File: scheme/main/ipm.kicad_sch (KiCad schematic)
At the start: 1 part

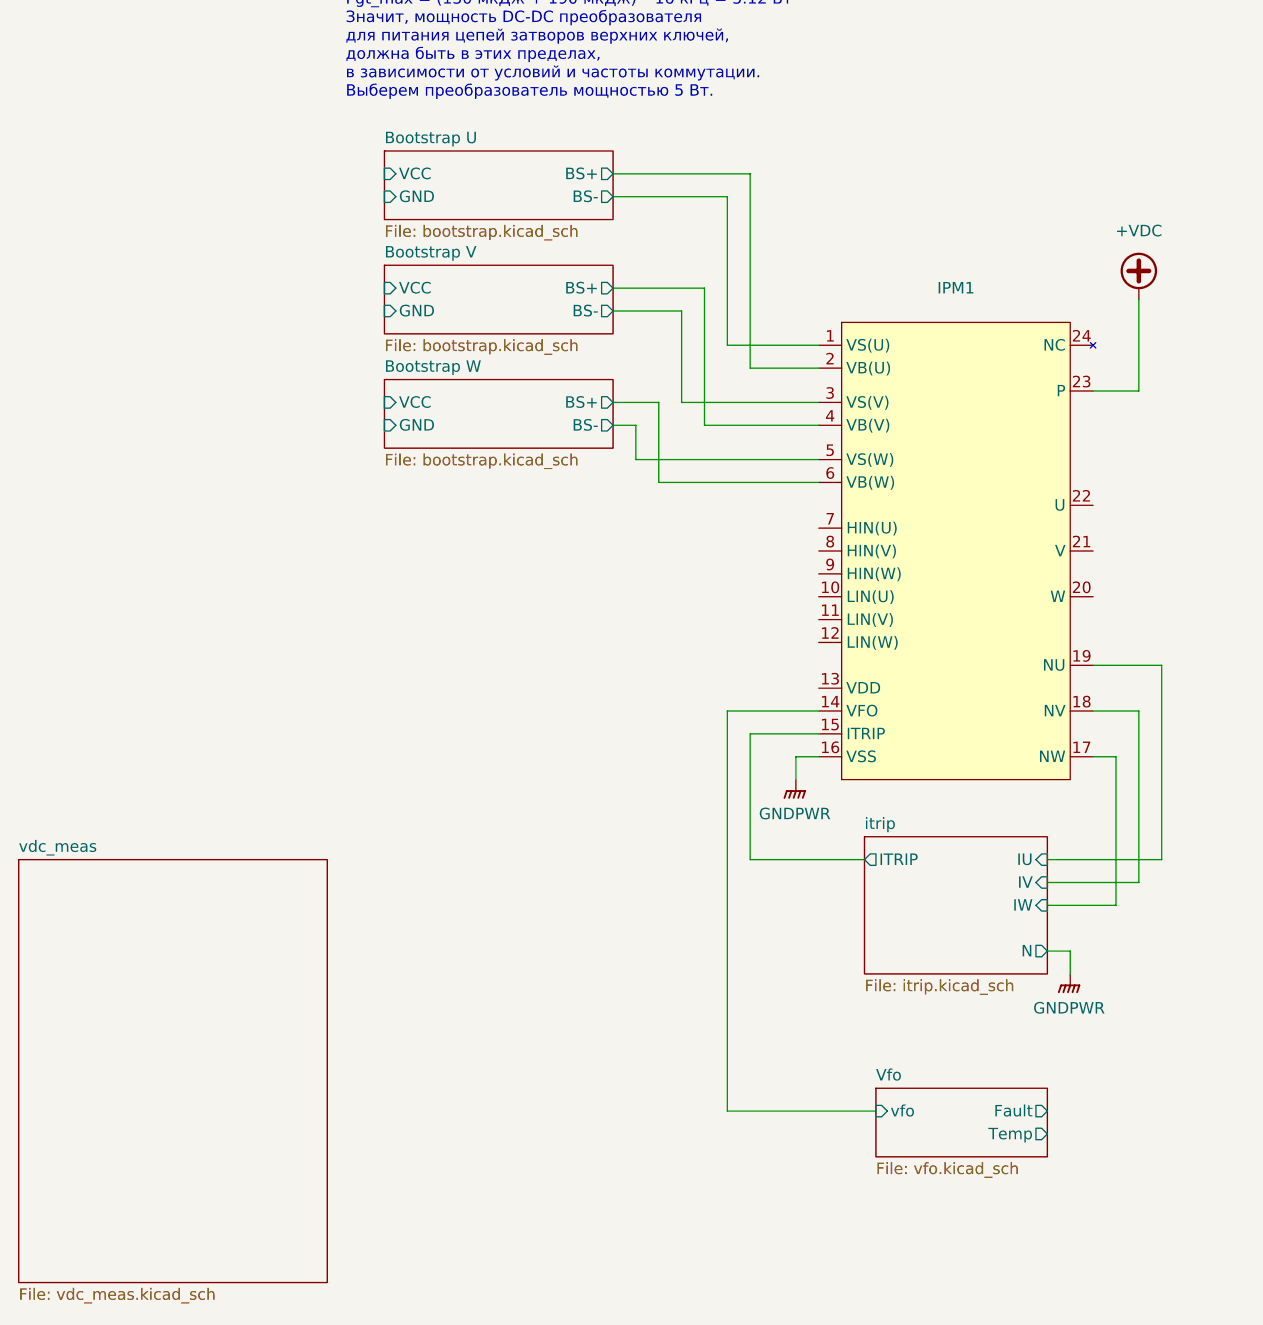
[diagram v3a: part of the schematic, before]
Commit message: bootstrap dc-dc add capacitors & more
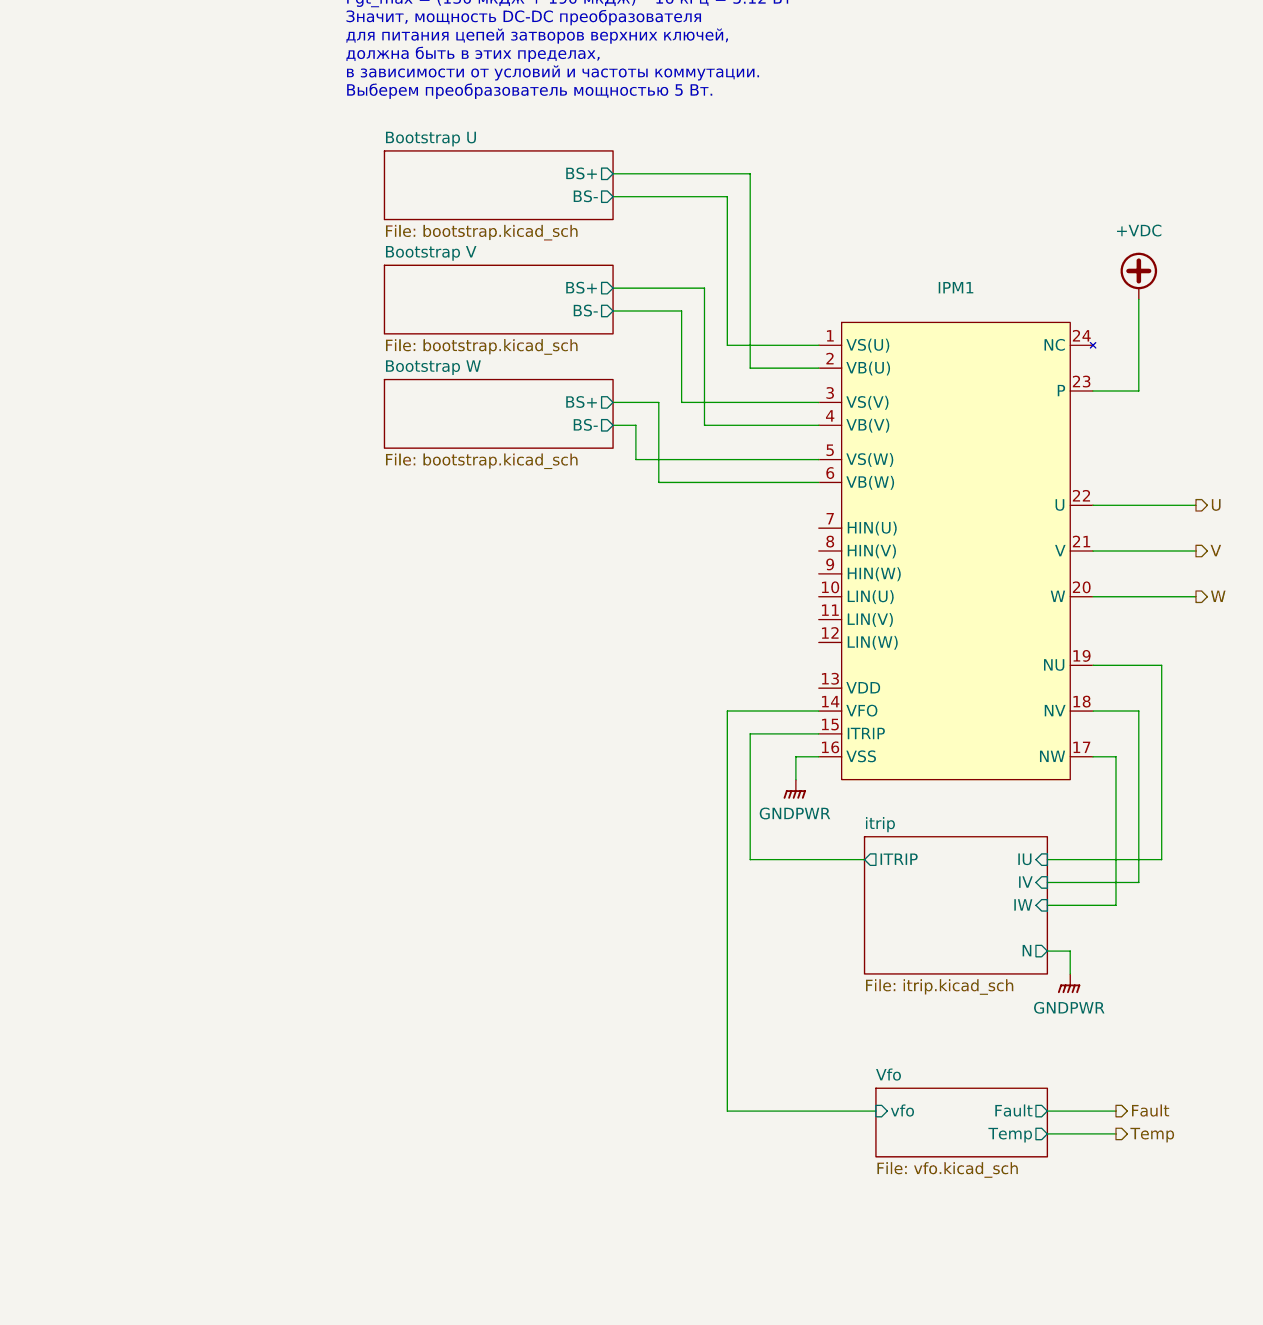
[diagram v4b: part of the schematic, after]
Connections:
- net W: now reaches IPM1.20 (W)
- net V: now reaches IPM1.21 (V)
- net U: now reaches IPM1.22 (U)
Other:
- removed sheet vdc_meas
- sheet Bootstrap U ports: added none; removed GND, VCC
- sheet Bootstrap V ports: added none; removed GND, VCC
- sheet Bootstrap W ports: added none; removed GND, VCC
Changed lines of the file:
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@@
+	(wire
+		(pts
+			(xy 200.66 114.3) (xy 212.09 114.3)
+		)
+		(stroke
+			(width 0)
+			(type default)
+		)
+	)
 	(wire
 		(pts
@@
 	(wire
 		(pts
+			(xy 200.66 119.38) (xy 212.09 119.38)
+		)
+		(stroke
+			(width 0)
+			(type default)
+		)
+	)
+	(wire
+		(pts
 			(xy 160.02 96.52) (xy 170.18 96.52)
 		)
@@
 	(wire
 		(pts
+			(xy 200.66 124.46) (xy 212.09 124.46)
+		)
+		(stroke
+			(width 0)
+			(type default)
+		)
+	)
+	(wire
+		(pts
 			(xy 162.56 139.7) (xy 170.18 139.7)
 		)
@@
 	(wire
 		(pts
+			(xy 195.58 184.15) (xy 203.2 184.15)
+		)
+		(stroke
+			(width 0)
+			(type default)
+		)
+	)
+	(wire
+		(pts
 			(xy 154.94 102.87) (xy 170.18 102.87)
 		)
@@
 		(pts
 			(xy 200.66 142.24) (xy 203.2 142.24)
+		)
+		(stroke
+			(width 0)
+			(type default)
+		)
+	)
+	(wire
+		(pts
+			(xy 195.58 181.61) (xy 203.2 181.61)
 		)
 		(stroke
@@
 		(exclude_from_sim no)
 		(at 117.602 49.022 0)
+		(effects
+			(font
+				(size 1.27 1.27)
+			)
+			(justify left)
+		)
+	)
+	(hierarchical_label "Fault"
+		(shape output)
+		(at 203.2 181.61 0)
+		(effects
+			(font
+				(size 1.27 1.27)
+			)
+			(justify left)
+		)
+	)
+	(hierarchical_label "W"
+		(shape output)
+		(at 212.09 124.46 0)
+		(effects
+			(font
+				(size 1.27 1.27)
+			)
+			(justify left)
+		)
+	)
+	(hierarchical_label "V"
+		(shape output)
+		(at 212.09 119.38 0)
+		(effects
+			(font
+				(size 1.27 1.27)
+			)
+			(justify left)
+		)
+	)
+	(hierarchical_label "U"
+		(shape output)
+		(at 212.09 114.3 0)
+		(effects
+			(font
+				(size 1.27 1.27)
+			)
+			(justify left)
+		)
+	)
+	(hierarchical_label "Temp"
+		(shape output)
+		(at 203.2 184.15 0)
 		(effects
 			(font
@@
 			)
 		)
-		(pin "VCC" input
-			(at 121.92 77.47 180)
-			(effects
-				(font
-					(size 1.27 1.27)
-				)
-				(justify left)
-			)
-		)
-		(pin "GND" input
-			(at 121.92 80.01 180)
-			(effects
-				(font
-					(size 1.27 1.27)
-				)
-				(justify left)
-			)
-		)
 		(pin "BS+" output
 			(at 147.32 77.47 0)
@@
 	)
 	(sheet
-		(at 81.28 153.67)
-		(size 34.29 46.99)
-		(fields_autoplaced yes)
-		(stroke
-			(width 0.1524)
-			(type solid)
-		)
-		(fill
-			(color 255 255 194 1.0000)
-		)
-		(property "Sheetname" "vdc_meas"
-			(at 81.28 152.9584 0)
-			(effects
-				(font
-					(size 1.27 1.27)
-				)
-				(justify left bottom)
-			)
-		)
-		(property "Sheetfile" "vdc_meas.kicad_sch"
-			(at 81.28 201.2446 0)
-			(effects
-				(font
-					(size 1.27 1.27)
-				)
-				(justify left top)
-			)
-		)
-		(instances
-			(project "main"
-				(path "/c11d1dbc-4db9-4712-8d1d-5f6f7086cded/5d407613-ca47-4478-86ea-137e1786be86"
-					(page "14")
-				)
-			)
-		)
-	)
-	(sheet
 		(at 121.92 100.33)
 		(size 25.4 7.62)
@@
 				)
 				(justify left top)
-			)
-		)
-		(pin "VCC" input
-			(at 121.92 102.87 180)
-			(effects
-				(font
-					(size 1.27 1.27)
-				)
-				(justify left)
-			)
-		)
-		(pin "GND" input
-			(at 121.92 105.41 180)
-			(effects
-				(font
-					(size 1.27 1.27)
-				)
-				(justify left)
 			)
 		)
@@
 			)
 		)
-		(pin "VCC" input
-			(at 121.92 90.17 180)
-			(effects
-				(font
-					(size 1.27 1.27)
-				)
-				(justify left)
-			)
-		)
-		(pin "GND" input
-			(at 121.92 92.71 180)
-			(effects
-				(font
-					(size 1.27 1.27)
-				)
-				(justify left)
-			)
-		)

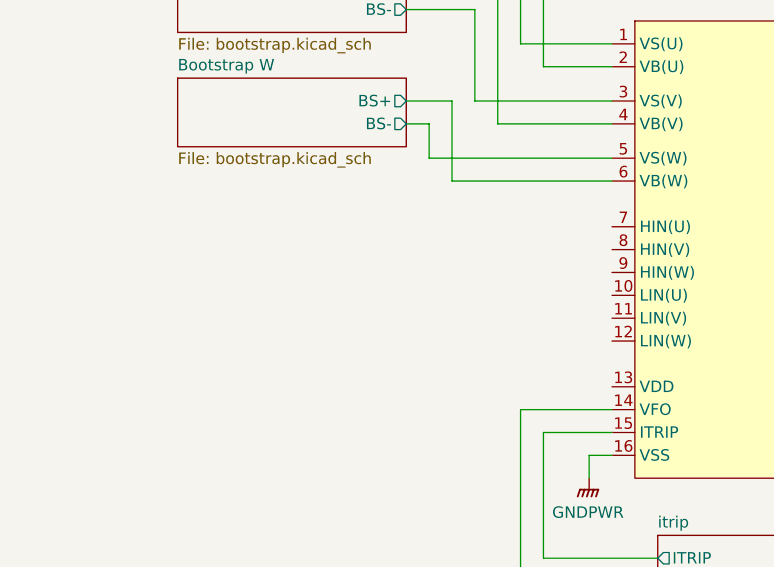
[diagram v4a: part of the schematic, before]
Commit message: control isolation schematic
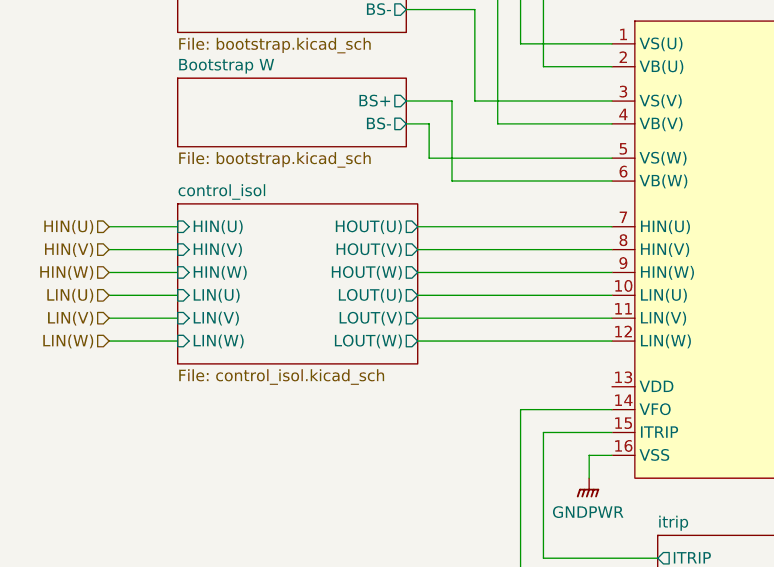
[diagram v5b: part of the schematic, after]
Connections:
- net control_isol/LOUT(U): now reaches IPM1.10 (LIN(U))
- net control_isol/LOUT(V): now reaches IPM1.11 (LIN(V))
- net control_isol/LOUT(W): now reaches IPM1.12 (LIN(W))
- net control_isol/HOUT(U): now reaches IPM1.7 (HIN(U))
- net control_isol/HOUT(V): now reaches IPM1.8 (HIN(V))
- net control_isol/HOUT(W): now reaches IPM1.9 (HIN(W))
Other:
- added sheet control_isol (control_isol.kicad_sch)

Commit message: power scheme
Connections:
- net +15V: now reaches IPM1.13 (VDD)
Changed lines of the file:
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@@
+	(wire
+		(pts
+			(xy 157.48 139.7) (xy 153.67 139.7)
+		)
+		(stroke
+			(width 0)
+			(type default)
+		)
+	)
 	(wire
 		(pts
@@
 	(wire
 		(pts
+			(xy 170.18 134.62) (xy 157.48 134.62)
+		)
+		(stroke
+			(width 0)
+			(type default)
+		)
+	)
+	(wire
+		(pts
 			(xy 148.59 129.54) (xy 170.18 129.54)
 		)
@@
 	(wire
 		(pts
+			(xy 153.67 137.16) (xy 153.67 139.7)
+		)
+		(stroke
+			(width 0)
+			(type default)
+		)
+	)
+	(wire
+		(pts
 			(xy 154.94 92.71) (xy 154.94 102.87)
 		)
@@
 		(pts
 			(xy 195.58 181.61) (xy 203.2 181.61)
+		)
+		(stroke
+			(width 0)
+			(type default)
+		)
+	)
+	(wire
+		(pts
+			(xy 157.48 134.62) (xy 157.48 139.7)
 		)
 		(stroke
@@
 		(shape input)
 		(at 114.3 116.84 180)
+		(fields_autoplaced yes)
 		(effects
 			(font
@@
 		(shape output)
 		(at 203.2 181.61 0)
+		(fields_autoplaced yes)
 		(effects
 			(font
@@
 		(shape output)
 		(at 212.09 124.46 0)
+		(fields_autoplaced yes)
 		(effects
 			(font
@@
 		(shape input)
 		(at 114.3 124.46 180)
+		(fields_autoplaced yes)
 		(effects
 			(font
@@
 		(shape input)
 		(at 114.3 127 180)
+		(fields_autoplaced yes)
 		(effects
 			(font
@@
 		(shape input)
 		(at 114.3 129.54 180)
+		(fields_autoplaced yes)
 		(effects
 			(font
@@
 		(shape output)
 		(at 212.09 119.38 0)
+		(fields_autoplaced yes)
 		(effects
 			(font
@@
 		(shape output)
 		(at 212.09 114.3 0)
+		(fields_autoplaced yes)
 		(effects
 			(font
@@
 		(shape input)
 		(at 114.3 119.38 180)
+		(fields_autoplaced yes)
 		(effects
 			(font
@@
 		(shape input)
 		(at 114.3 121.92 180)
+		(fields_autoplaced yes)
 		(effects
 			(font
@@
 		(shape output)
 		(at 203.2 184.15 0)
+		(fields_autoplaced yes)
 		(effects
 			(font
@@
 					(unit 1)
 				)
+			)
+		)
+	)
+	(symbol
+		(lib_id "power:+15V")
+		(at 153.67 137.16 0)
+		(unit 1)
+		(exclude_from_sim no)
+		(in_bom yes)
+		(on_board yes)
+		(dnp no)
+		(fields_autoplaced yes)
+		(property "Reference" "#PWR084"
+			(at 153.67 140.97 0)
+			(effects
+				(font
+					(size 1.27 1.27)
+				)
+				(hide yes)
+			)
+		)
+		(property "Value" "+15V"
+			(at 153.67 132.08 0)
+			(effects
+				(font
+					(size 1.27 1.27)
+				)
+			)
+		)
+		(property "Footprint" ""
+			(at 153.67 137.16 0)
+			(effects
+				(font
+					(size 1.27 1.27)
+				)
+				(hide yes)
+			)
+		)
+		(property "Datasheet" ""
+			(at 153.67 137.16 0)
+			(effects
+				(font
+					(size 1.27 1.27)
+				)
+				(hide yes)
+			)
+		)
+		(property "Description" "Power symbol creates a global label with name \"+15V\""
+			(at 153.67 137.16 0)
+			(effects
+				(font
+					(size 1.27 1.27)
+				)
+				(hide yes)
+			)
+		)
+		(pin "1"
+		)
+		(instances
+			(project ""
+				(path "/c11d1dbc-4db9-4712-8d1d-5f6f7086cded/5d407613-ca47-4478-86ea-137e1786be86"
+					(reference "#PWR084")
+					(unit 1)
+				)

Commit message: ipm snubber capacitor
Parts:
- added C83: 5uF, Capacitor_THT:C_Rect_L31.5mm_W15.0mm_P27.50mm_MKS4, symbol Device:C
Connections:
- net +VDC: now also C83.1
- net GNDPWR: now also C83.2
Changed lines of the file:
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@@
 	(generator_version "8.0")
 	(paper "A3")
+	(junction
+		(at 205.74 96.52)
+		(diameter 0)
+		(color 0 0 0 0)
+	)
 	(wire
 		(pts
@@
 	(wire
 		(pts
-			(xy 205.74 91.44) (xy 205.74 101.6)
+			(xy 205.74 91.44) (xy 205.74 96.52)
 		)
 		(stroke
@@
 	(wire
 		(pts
+			(xy 215.9 105.41) (xy 215.9 106.68)
+		)
+		(stroke
+			(width 0)
+			(type default)
+		)
+	)
+	(wire
+		(pts
 			(xy 160.02 137.16) (xy 160.02 181.61)
 		)
@@
 	(wire
 		(pts
+			(xy 205.74 96.52) (xy 215.9 96.52)
+		)
+		(stroke
+			(width 0)
+			(type default)
+		)
+	)
+	(wire
+		(pts
 			(xy 148.59 129.54) (xy 170.18 129.54)
 		)
@@
 	(wire
 		(pts
+			(xy 215.9 97.79) (xy 215.9 96.52)
+		)
+		(stroke
+			(width 0)
+			(type default)
+		)
+	)
+	(wire
+		(pts
 			(xy 195.58 181.61) (xy 203.2 181.61)
 		)
@@
 		(pts
 			(xy 162.56 99.06) (xy 170.18 99.06)
+		)
+		(stroke
+			(width 0)
+			(type default)
+		)
+	)
+	(wire
+		(pts
+			(xy 205.74 96.52) (xy 205.74 101.6)
 		)
 		(stroke
@@
 					(unit 1)
 				)
+			)
+		)
+	)
+	(symbol
+		(lib_id "Device:C")
+		(at 215.9 101.6 0)
+		(unit 1)
+		(exclude_from_sim no)
+		(in_bom yes)
+		(on_board yes)
+		(dnp no)
+		(fields_autoplaced yes)
+		(property "Reference" "C83"
+			(at 219.71 100.3299 0)
+			(effects
+				(font
+					(size 1.27 1.27)
+				)
+				(justify left)
+			)
+		)
+		(property "Value" "5uF"
+			(at 219.71 102.8699 0)
+			(effects
+				(font
+					(size 1.27 1.27)
+				)
+				(justify left)
+			)
+		)
+		(property "Footprint" "Capacitor_THT:C_Rect_L31.5mm_W15.0mm_P27.50mm_MKS4"
+			(at 216.8652 105.41 0)
+			(effects
+				(font
+					(size 1.27 1.27)
+				)
+				(hide yes)
+			)
+		)
+		(property "Datasheet" "https://doc.platan.ru/pdf/datasheets/epcos/MKP_B32774_778-525242.pdf"
+			(at 215.9 101.6 0)
+			(effects
+				(font
+					(size 1.27 1.27)
+				)
+				(hide yes)
+			)
+		)
+		(property "Description" "B32774D8505K"
+			(at 215.9 101.6 0)
+			(effects
+				(font
+					(size 1.27 1.27)
+				)
+				(hide yes)
+			)
+		)
+		(pin "2"
+		)
+		(pin "1"
+		)
+		(instances
+			(project ""
+				(path "/c11d1dbc-4db9-4712-8d1d-5f6f7086cded/5d407613-ca47-4478-86ea-137e1786be86"
+					(reference "C83")
+					(unit 1)
+				)
+			)
+		)
+	)
+	(symbol
+		(lib_id "power:GNDPWR")
+		(at 215.9 106.68 0)
+		(unit 1)
+		(exclude_from_sim no)
+		(in_bom yes)
+		(on_board yes)
+		(dnp no)
+		(property "Reference" "#PWR085"
+			(at 215.9 111.76 0)
+			(effects
+				(font
+					(size 1.27 1.27)
+				)
+				(hide yes)
+			)
+		)
+		(property "Value" "GNDPWR"
+			(at 215.773 110.49 0)
+			(effects
+				(font
+					(size 1.27 1.27)
+				)
+			)
+		)
+		(property "Footprint" ""
+			(at 215.9 107.95 0)
+			(effects
+				(font
+					(size 1.27 1.27)
+				)
+				(hide yes)
+			)
+		)
+		(property "Datasheet" ""
+			(at 215.9 107.95 0)
+			(effects
+				(font
+					(size 1.27 1.27)
+				)
+				(hide yes)
+			)
+		)
+		(property "Description" "Power symbol creates a global label with name \"GNDPWR\" , global ground"
+			(at 215.9 106.68 0)
+			(effects
+				(font
+					(size 1.27 1.27)
+				)
+				(hide yes)
+			)
+		)
+		(pin "1"
+		)
+		(instances
+			(project "main"
+				(path "/c11d1dbc-4db9-4712-8d1d-5f6f7086cded/5d407613-ca47-4478-86ea-137e1786be86"
+					(reference "#PWR085")
+					(unit 1)
+				)

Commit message: separate hi power & signal gnd
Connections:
- net GNDPWR: no longer IPM1.16 (VSS)
- new net GNDH: IPM1.16 (VSS)
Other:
- sheet itrip ports: added none; removed N
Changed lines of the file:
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@@
-	(wire
-		(pts
-			(xy 195.58 163.83) (xy 198.12 163.83)
-		)
-		(stroke
-			(width 0)
-			(type default)
-		)
-	)
 	(wire
 		(pts
@@
 		(pts
 			(xy 152.4 111.76) (xy 170.18 111.76)
-		)
-		(stroke
-			(width 0)
-			(type default)
-		)
-	)
-	(wire
-		(pts
-			(xy 198.12 163.83) (xy 198.12 166.37)
 		)
 		(stroke
@@
 	)
 	(symbol
-		(lib_id "power:GNDPWR")
+		(lib_id "main:GNDH")
 		(at 167.64 144.78 0)
 		(unit 1)
@@
 		(on_board yes)
 		(dnp no)
+		(fields_autoplaced yes)
 		(property "Reference" "#PWR03"
+			(at 167.64 151.13 0)
+			(effects
+				(font
+					(size 1.27 1.27)
+				)
+				(hide yes)
+			)
+		)
+		(property "Value" "GNDH"
 			(at 167.64 149.86 0)
 			(effects
@@
 					(size 1.27 1.27)
 				)
-				(hide yes)
-			)
-		)
-		(property "Value" "GNDPWR"
-			(at 167.513 148.59 0)
-			(effects
-				(font
-					(size 1.27 1.27)
-				)
 			)
 		)
 		(property "Footprint" ""
-			(at 167.64 146.05 0)
+			(at 167.64 144.78 0)
 			(effects
 				(font
@@
 		)
 		(property "Datasheet" ""
-			(at 167.64 146.05 0)
-			(effects
-				(font
-					(size 1.27 1.27)
-				)
-				(hide yes)
-			)
-		)
-		(property "Description" "Power symbol creates a global label with name \"GNDPWR\" , global ground"
+			(at 167.64 144.78 0)
+			(effects
+				(font
+					(size 1.27 1.27)
+				)
+				(hide yes)
+			)
+		)
+		(property "Description" "Power symbol creates a global label with name \"GNDH\" , hi ground"
 			(at 167.64 144.78 0)
 			(effects
@@
 				(path "/c11d1dbc-4db9-4712-8d1d-5f6f7086cded/5d407613-ca47-4478-86ea-137e1786be86"
 					(reference "#PWR03")
-					(unit 1)
-				)
-			)
-		)
-	)
-	(symbol
-		(lib_id "power:GNDPWR")
-		(at 198.12 166.37 0)
-		(unit 1)
-		(exclude_from_sim no)
-		(in_bom yes)
-		(on_board yes)
-		(dnp no)
-		(property "Reference" "#PWR04"
-			(at 198.12 171.45 0)
-			(effects
-				(font
-					(size 1.27 1.27)
-				)
-				(hide yes)
-			)
-		)
-		(property "Value" "GNDPWR"
-			(at 197.993 170.18 0)
-			(effects
-				(font
-					(size 1.27 1.27)
-				)
-			)
-		)
-		(property "Footprint" ""
-			(at 198.12 167.64 0)
-			(effects
-				(font
-					(size 1.27 1.27)
-				)
-				(hide yes)
-			)
-		)
-		(property "Datasheet" ""
-			(at 198.12 167.64 0)
-			(effects
-				(font
-					(size 1.27 1.27)
-				)
-				(hide yes)
-			)
-		)
-		(property "Description" "Power symbol creates a global label with name \"GNDPWR\" , global ground"
-			(at 198.12 166.37 0)
-			(effects
-				(font
-					(size 1.27 1.27)
-				)
-				(hide yes)
-			)
-		)
-		(pin "1"
-		)
-		(instances
-			(project "main"
-				(path "/c11d1dbc-4db9-4712-8d1d-5f6f7086cded/5d407613-ca47-4478-86ea-137e1786be86"
-					(reference "#PWR04")
 					(unit 1)
 				)
@@
 			(effects
 				(font
-					(size 1.27 1.27)
-				)
-				(justify right)
-			)
-		)
-		(pin "N" output
-			(at 195.58 163.83 0)
-			(effects
-				(font
